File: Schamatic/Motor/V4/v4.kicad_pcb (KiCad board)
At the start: 4 copper layers, 40 x 25 mm, 45 parts, among them J1 SWD, J10 GND, J11 V, J12 U, J13 W, J2 SPI, J3 RS485, J4 RS485, J5 12, J6 12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

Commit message: ordered controller
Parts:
- removed C3: 1uF, Capacitors_SMD:C_0805
- removed R1: 47K, Resistors_SMD:R_0805
- removed R2: 3K, Resistors_SMD:R_0805
- added J14: A0, Pin_Headers:Pin_Header_Straight_1x01_Pitch2.54mm, F.Cu at (109.4, 91.2)
- moved C6 31.5 mm to (133.3, 89.9), turned to 90 degrees
- moved R7 30.7 mm to (133.1, 86.9)
- moved R8 28.7 mm to (131.2, 89.9), turned to 270 degrees
- moved C5 26.0 mm to (128.9, 90.0), turned to 90 degrees
- moved R5 25.6 mm to (128.8, 87.2)
- moved R6 23.6 mm to (126.9, 90.0), turned to 270 degrees
- moved R3 23.3 mm to (124.3, 80.2), turned to 270 degrees
- moved J2 23.2 mm to (117.3, 94.0), turned to 270 degrees
- moved C4 23.1 mm to (122.7, 80.2), turned to 270 degrees
- moved D3 22.8 mm to (133.2, 94.2), turned to 180 degrees
- moved D1 21.8 mm to (108.6, 76.1)
- moved R4 21.2 mm to (120.0, 81.3), turned to 90 degrees
- moved R9 20.9 mm to (113.2, 76.1)
- moved J1 20.1 mm to (104.5, 79.4), turned to 0 degrees
- moved C1 17.5 mm to (112.2, 78.5), turned to 90 degrees
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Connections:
- J2 pad 1: +3V3 -> MOSI
- J2 pad 2: Earth -> MISO
- J2 pad 3: MOSI -> SCK
- J2 pad 4: MISO -> CS
- J2 pad 5: SCK -> Earth
- J2 pad 6: CS -> +3V3
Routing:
- net Earth: track 22.2 -> 93.2 mm, vias 0 -> 13
- net +3V3: track 3.98 -> 74.9 mm, vias 0 -> 2
- net O3: track 12.4 -> 39.3 mm
- net O2: track 10.2 -> 35.8 mm
- net DE: track 0.00 -> 24.8 mm, vias 0 -> 2
- net Net-(D3-Pad2): track 0.00 -> 22.0 mm
- net +12V: track 22.5 -> 44.4 mm, vias 0 -> 1
- net NRST: track 24.2 -> 8.86 mm, vias 2 -> 0
- net Net-(SW1-Pad1): track 0.00 -> 15.1 mm, vias 0 -> 2
- net H3: track 10.9 -> 25.9 mm
- net Net-(Q2-Pad4): track 0.00 -> 14.2 mm, vias 0 -> 1
- net H2: track 7.80 -> 20.9 mm
- net Net-(SW2-Pad1): track 0.00 -> 12.0 mm, vias 0 -> 2
- net Net-(Q4-Pad4): track 0.00 -> 10.6 mm, vias 0 -> 1
- net Net-(Q6-Pad4): track 0.00 -> 10.5 mm, vias 0 -> 1
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- added copper zone on B.Cu, net Earth
- added copper zone on B.Cu, net O1
- added copper zone on B.Cu, net O2
- added copper zone on B.Cu, net O3
- removed copper zone on B.Cu, net Net-(D3-Pad2)
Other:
- board size 40 x 25 mm -> 37.1 x 20.3 mm
- copper layers 4 -> 2
- net class Default: clearance 0.2 -> 0.13
- rule trace_clearance: 0.2 -> 0.13
- board text added: "3.3"
- board text added: "CS"
- board text added: "CSK"
- board text added: "GND"
- board text added: "MISO"
- board text added: "MOSI"
- board text added: "NRST"
- board text added: "SWDCLK"
- board text added: "SWDIO"

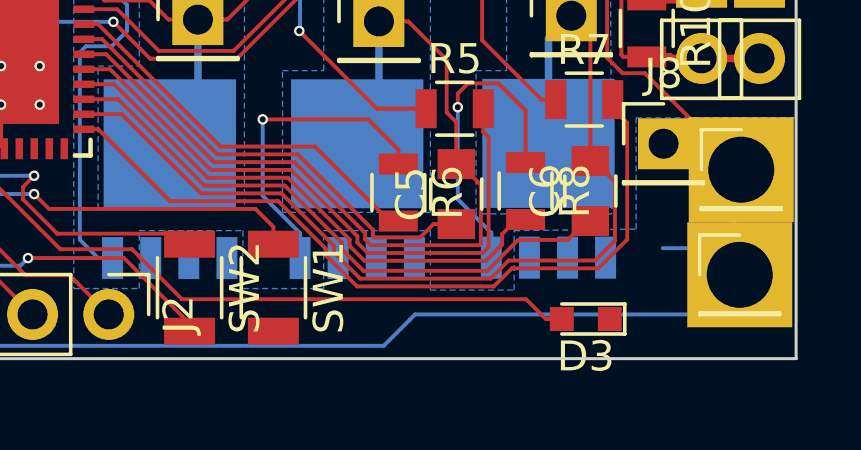
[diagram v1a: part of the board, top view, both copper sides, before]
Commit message: button press and external clock
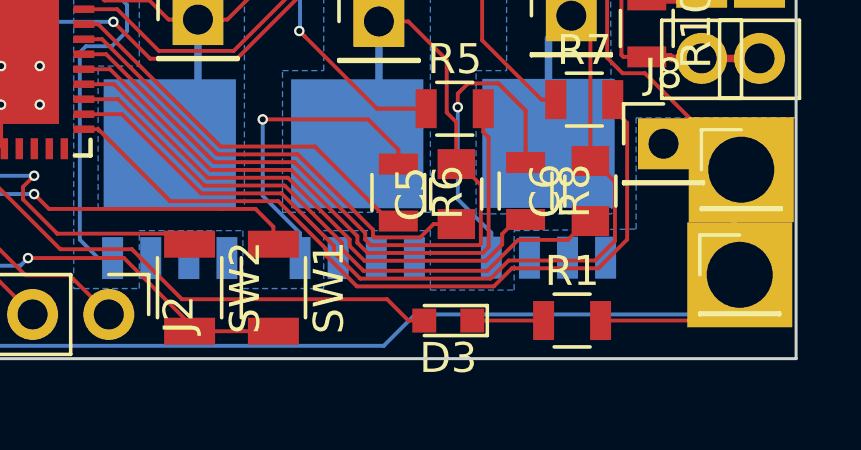
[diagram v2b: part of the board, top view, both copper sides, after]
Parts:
- added R1: 120, Resistors_SMD:R_0805, F.Cu at (132.7, 94.2)
- C1: value 47uF -> 100uF
- C2: value 47uF -> 22uF
- moved D3 4.59 mm to (128.6, 94.2)
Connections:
- D3 pad 1: Earth -> Net-(D3-Pad1)
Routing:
- net Net-(D3-Pad2): track 22.0 -> 17.4 mm
- net Earth: track 93.2 -> 96.9 mm
- net +3V3: track 74.9 -> 77.7 mm
- net Net-(D3-Pad1): track 0.00 -> 2.38 mm
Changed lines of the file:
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@@
 (kicad_pcb (version 4) (host pcbnew 4.0.6)
   (general
-    (links 115)
-    (no_connects 0)
+    (links 116)
+    (no_connects 2)
     (area 103.073999 75.133999 140.258001 95.554001)
     (thickness 1.6)
     (drawings 14)
-    (tracks 465)
+    (tracks 470)
     (zones 0)
-    (modules 43)
-    (nets 56)
+    (modules 44)
+    (nets 57)
   )
   (page A4)
@@
   (net 54 "Net-(U1-Pad47)")
   (net 55 "Net-(J14-Pad1)")
+  (net 56 "Net-(D3-Pad1)")
   (net_class Default "This is the default net class."
     (clearance 0.13)
@@
     (add_net "Net-(D1-Pad1)")
     (add_net "Net-(D2-Pad1)")
+    (add_net "Net-(D3-Pad1)")
     (add_net "Net-(D3-Pad2)")
     (add_net "Net-(J14-Pad1)")
@@
   )
   (module LEDs:LED_0603 (layer F.Cu)
-    (at 133.1976 94.1832 180)
+    (at 128.6128 94.234 180)
     (descr "LED 0603 smd package")
     (tags "LED led 0603 SMD smd SMT smt smdled SMDLED smtled SMTLED")
@@
       (net 12 "Net-(D3-Pad2)"))
     (pad 1 smd rect (at -0.8 0) (size 0.8 0.8) (layers F.Cu F.Paste F.Mask)
-      (net 2 Earth))
+      (net 56 "Net-(D3-Pad1)"))
     (model ${KISYS3DMOD}/LEDs.3dshapes/LED_0603.wrl
       (at (xyz 0 0 0))
@@
       (effects (font (size 1 1) (thickness 0.15)))
     )
-    (fp_text value 47uF (at 0 1.75 90) (layer F.Fab) hide
+    (fp_text value 100uF (at 0 1.75 90) (layer F.Fab) hide
       (effects (font (size 1 1) (thickness 0.15)))
     )
@@
       (effects (font (size 1 1) (thickness 0.15)))
     )
-    (fp_text value 47uF (at 0 1.75 90) (layer F.Fab) hide
+    (fp_text value 22uF (at 0 1.75 90) (layer F.Fab) hide
       (effects (font (size 1 1) (thickness 0.15)))
     )
@@
     )
   )
+  (module Resistors_SMD:R_0805 (layer F.Cu)
+    (at 132.7404 94.234)
+    (descr "Resistor SMD 0805, reflow soldering, Vishay (see dcrcw.pdf)")
+    (tags "resistor 0805")
+    (attr smd)
+    (fp_text reference R1 (at 0 -1.65) (layer F.SilkS)
+      (effects (font (size 1 1) (thickness 0.15)))
+    )
+    (fp_text value 120 (at 0 1.75) (layer F.Fab)
+      (effects (font (size 1 1) (thickness 0.15)))
+    )
+    (fp_text user %R (at 2.286 0.5588) (layer F.Fab)
+      (effects (font (size 0.5 0.5) (thickness 0.075)))
+    )
+    (fp_line (start -1 0.62) (end -1 -0.62) (layer F.Fab) (width 0.1))
+    (fp_line (start 1 0.62) (end -1 0.62) (layer F.Fab) (width 0.1))
+    (fp_line (start 1 -0.62) (end 1 0.62) (layer F.Fab) (width 0.1))
+    (fp_line (start -1 -0.62) (end 1 -0.62) (layer F.Fab) (width 0.1))
+    (fp_line (start 0.6 0.88) (end -0.6 0.88) (layer F.SilkS) (width 0.12))
+    (fp_line (start -0.6 -0.88) (end 0.6 -0.88) (layer F.SilkS) (width 0.12))
+    (fp_line (start -1.55 -0.9) (end 1.55 -0.9) (layer F.CrtYd) (width 0.05))
+    (fp_line (start -1.55 -0.9) (end -1.55 0.9) (layer F.CrtYd) (width 0.05))
+    (fp_line (start 1.55 0.9) (end 1.55 -0.9) (layer F.CrtYd) (width 0.05))
+    (fp_line (start 1.55 0.9) (end -1.55 0.9) (layer F.CrtYd) (width 0.05))
+    (pad 1 smd rect (at -0.95 0) (size 0.7 1.3) (layers F.Cu F.Paste F.Mask)
+      (net 56 "Net-(D3-Pad1)"))
+    (pad 2 smd rect (at 0.95 0) (size 0.7 1.3) (layers F.Cu F.Paste F.Mask)
+      (net 2 Earth))
+    (model ${KISYS3DMOD}/Resistors_SMD.3dshapes/R_0805.wrl
+      (at (xyz 0 0 0))
+      (scale (xyz 1 1 1))
+      (rotate (xyz 0 0 0))
+    )
+  )
   (gr_text GND (at 107.0356 91.5924 270) (layer B.SilkS)
     (effects (font (size 1 1) (thickness 0.25)) (justify mirror))
@@
   (gr_line (start 103.124 75.184) (end 140.208 75.184) (angle 90) (layer Edge.Cuts) (width 0.1))
   (gr_line (start 103.124 95.504) (end 103.124 75.184) (angle 90) (layer Edge.Cuts) (width 0.1))
+  (segment (start 122.7836 94.5896) (end 121.8036 94.5896) (width 0.13) (layer F.Cu) (net 1))
+  (segment (start 121.8036 94.5896) (end 119.9896 94.5896) (width 0.13) (layer F.Cu) (net 1))
   (segment (start 119.9896 94.5896) (end 119.9896 94.3356) (width 0.13) (layer F.Cu) (net 1))
   (segment (start 119.9896 94.3356) (end 117.8052 92.1512) (width 0.13) (layer F.Cu) (net 1))
@@
   (segment (start 134.6784 77.9798) (end 133.4574 76.7588) (width 0.25) (layer F.Cu) (net 1))
   (segment (start 133.4574 76.7588) (end 133.08 76.7588) (width 0.25) (layer F.Cu) (net 1))
+  (segment (start 133.6904 94.234) (end 136.8044 94.234) (width 0.13) (layer F.Cu) (net 2))
+  (segment (start 136.8044 94.234) (end 138.3284 92.71) (width 0.13) (layer F.Cu) (net 2))
   (segment (start 107.1372 94.0308) (end 108.182201 95.075801) (width 0.13) (layer B.Cu) (net 2))
   (segment (start 108.182201 95.075801) (end 126.462999 95.075801) (width 0.13) (layer B.Cu) (net 2))
@@
   (segment (start 138.176 87.884) (end 138.176 90.932) (width 0.13) (layer B.Cu) (net 2))
   (segment (start 138.176 90.932) (end 137.287 91.821) (width 0.13) (layer B.Cu) (net 2))
-  (segment (start 137.287 91.821) (end 135.763 91.821) (width 0.13) (layer B.Cu) (net 2))
   (segment (start 108.475126 84.85665) (end 109.18415 84.85665) (width 0.13) (layer F.Cu) (net 3))
   (segment (start 107.0864 86.5792) (end 107.0864 86.245376) (width 0.13) (layer F.Cu) (net 3))
@@
   (segment (start 107.516 76.1048) (end 107.5096 76.0984) (width 0.13) (layer F.Cu) (net 10))
   (segment (start 114.046 78.0924) (end 114.046 76.2356) (width 0.25) (layer F.Cu) (net 11))
+  (segment (start 127.8128 94.234) (end 127.2828 94.234) (width 0.13) (layer F.Cu) (net 12))
+  (segment (start 127.2828 94.234) (end 126.5716 93.5228) (width 0.13) (layer F.Cu) (net 12))
+  (segment (start 126.5716 93.5228) (end 119.7356 93.5228) (width 0.13) (layer F.Cu) (net 12))
   (segment (start 113.31415 88.50665) (end 113.31415 89.489865) (width 0.13) (layer F.Cu) (net 12))
   (segment (start 113.31415 89.489865) (end 115.680733 91.856448) (width 0.13) (layer F.Cu) (net 12))
   (segment (start 115.680733 91.856448) (end 118.069248 91.856448) (width 0.13) (layer F.Cu) (net 12))
   (segment (start 118.069248 91.856448) (end 119.7356 93.5228) (width 0.13) (layer F.Cu) (net 12))
-  (segment (start 119.7356 93.5228) (end 131.2072 93.5228) (width 0.13) (layer F.Cu) (net 12))
-  (segment (start 131.2072 93.5228) (end 131.8676 94.1832) (width 0.13) (layer F.Cu) (net 12))
-  (segment (start 131.8676 94.1832) (end 132.3976 94.1832) (width 0.13) (layer F.Cu) (net 12))
   (segment (start 109.66415 85.35665) (end 109.18415 85.35665) (width 0.13) (layer F.Cu) (net 13))
   (segment (start 107.696 87.4268) (end 106.2736 87.4268) (width 0.13) (layer F.Cu) (net 13))
@@
   (segment (start 109.18415 87.35665) (end 109.119149 87.421651) (width 0.13) (layer F.Cu) (net 55))
   (segment (start 109.119149 87.421651) (end 109.119149 89.952749) (width 0.13) (layer F.Cu) (net 55))
+  (segment (start 129.4128 94.234) (end 129.9428 94.234) (width 0.13) (layer F.Cu) (net 56))
+  (segment (start 129.9428 94.234) (end 131.7904 94.234) (width 0.13) (layer F.Cu) (net 56))
   (zone (net 23) (net_name +12V) (layer B.Cu) (hatch edge 0.508)
     (connect_pads yes (clearance 0.1))
